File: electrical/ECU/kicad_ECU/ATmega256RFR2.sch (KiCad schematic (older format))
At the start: 29 parts

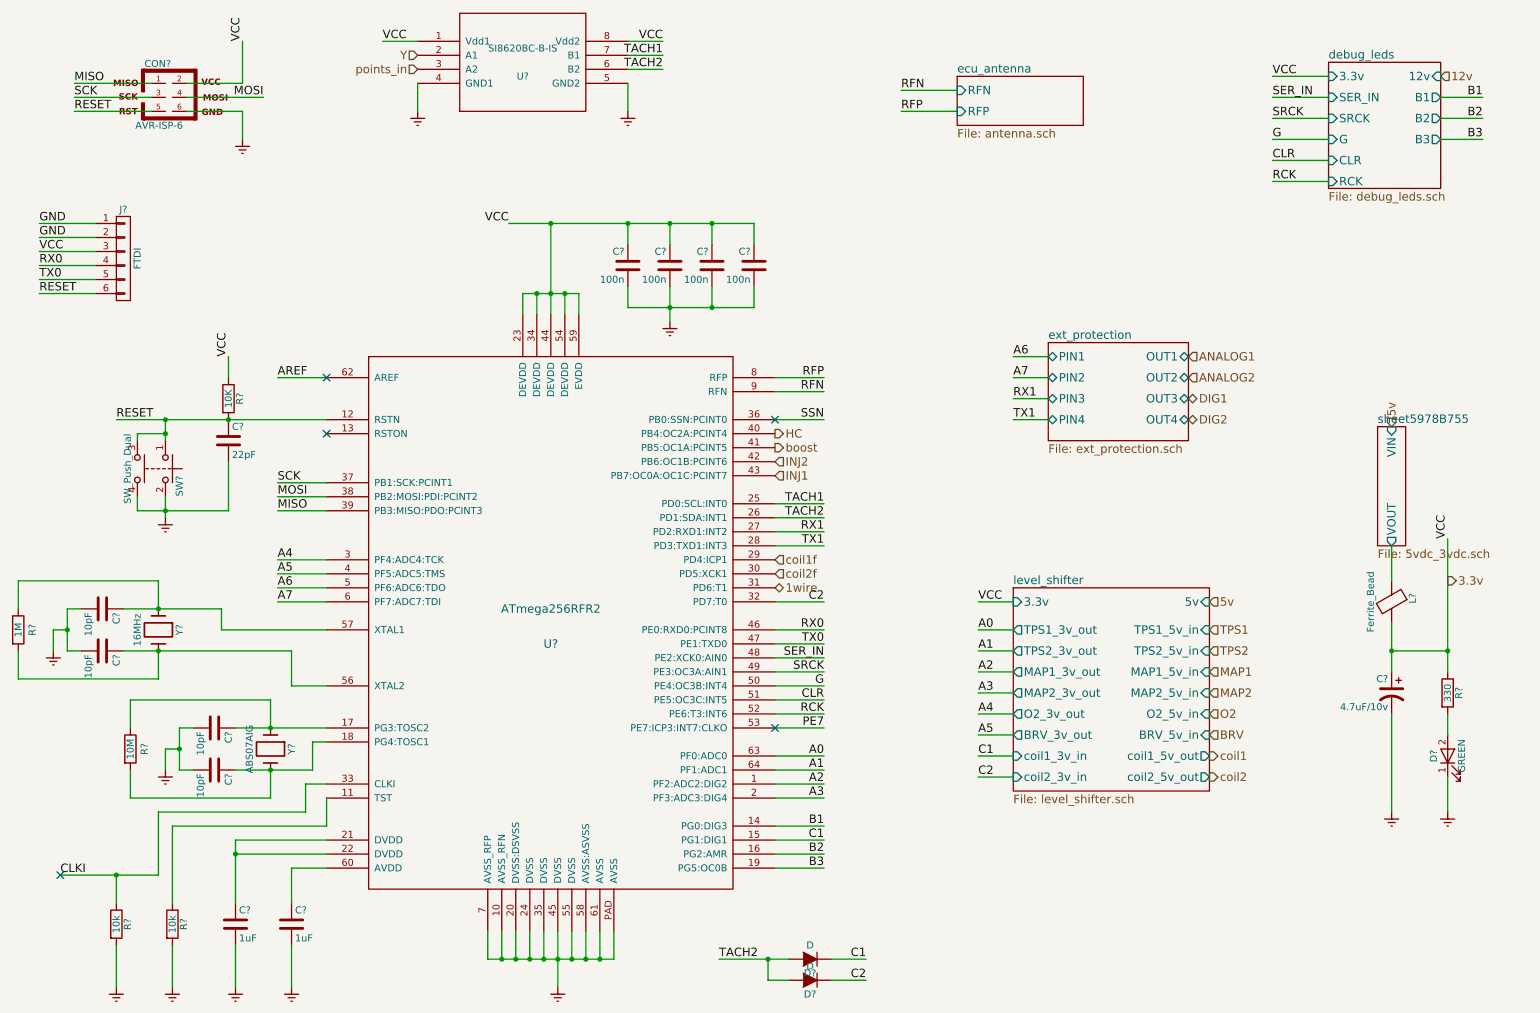
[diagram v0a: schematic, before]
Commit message: fixed some naming errors and initial round of double checking
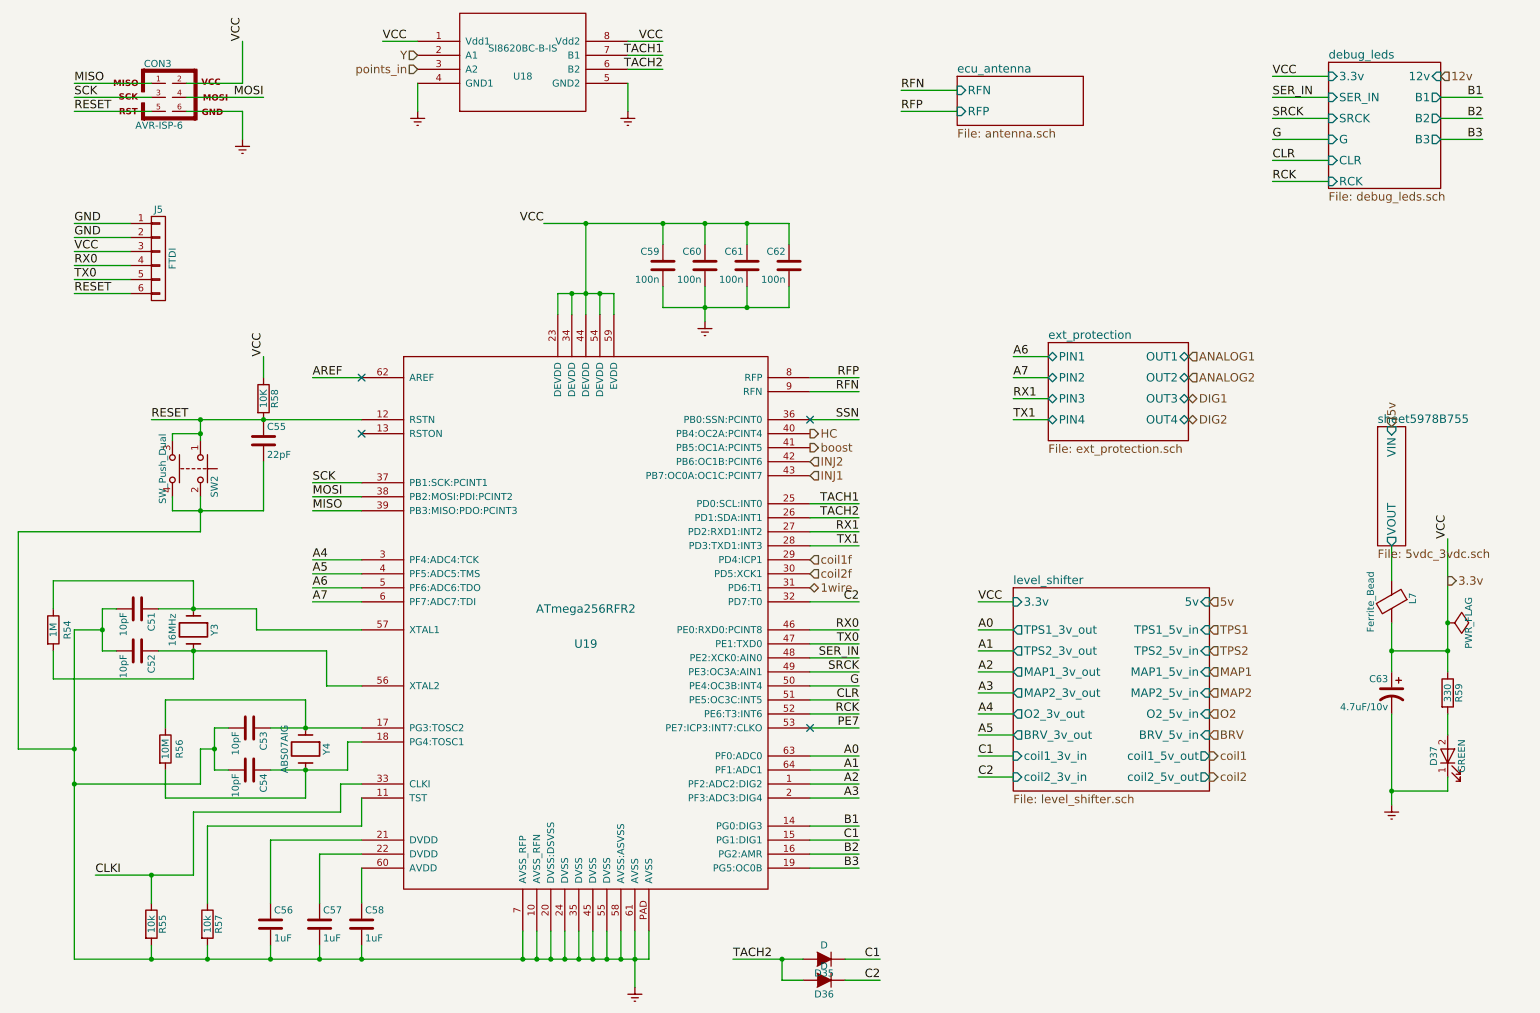
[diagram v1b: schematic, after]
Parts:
- added C57: 1uF, symbol C
- gave numbers to parts that had none: 29
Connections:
- net Earth: now also C57.2
- net at C56.1, U19.21 (DVDD): no longer U19.22 (DVDD)
- new net: C57.1, U19.22 (DVDD)
- no-connect marks 5 -> 4
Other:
- moved on the sheet: C51, C52, C53, C54, C55, C56, C58, C59, C60, C61, C62, D35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
